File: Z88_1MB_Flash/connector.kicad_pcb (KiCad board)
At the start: 2 copper layers, 50.6 x 53.5 mm, 10 parts, among them J1 Conn_Z88, U1 AM29F080-120EC

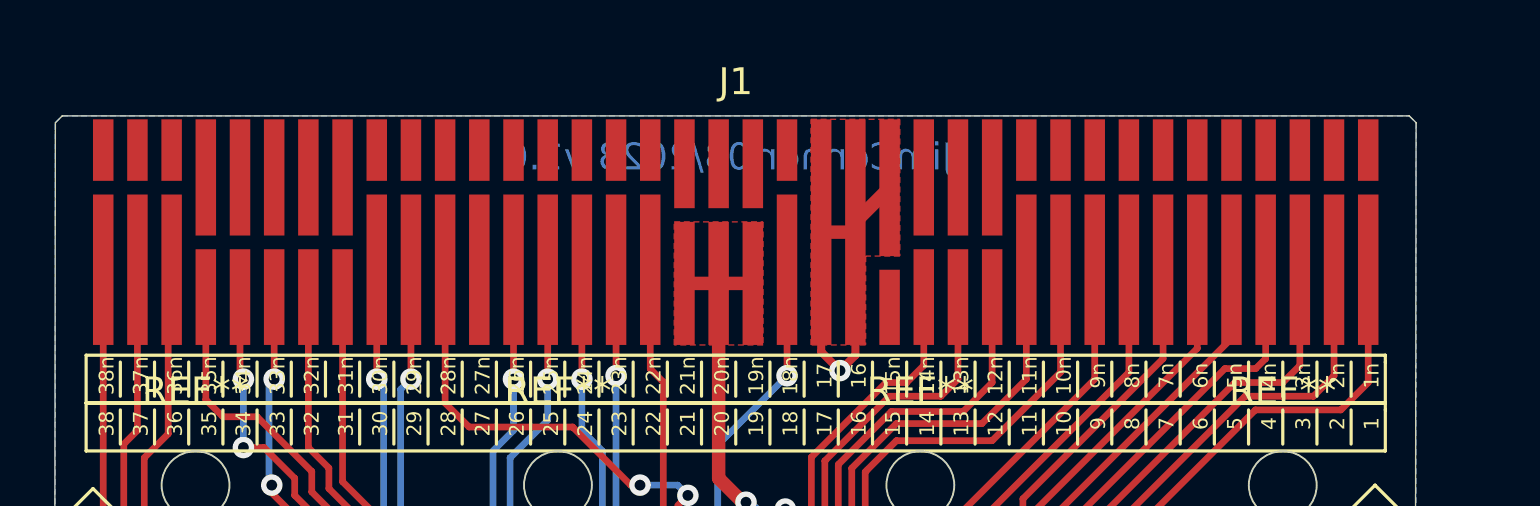
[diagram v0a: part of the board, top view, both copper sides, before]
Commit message: Correct pitch on Z88_connector.
Pads now spaced on 1.25mm instead of 1.27mm spacing.
Pad sizes changed to match the genuine Cambridge cartridge I have.
Sizes nicely in convienent 2m,3mm, 4mm sizing with 0.5mm gap.
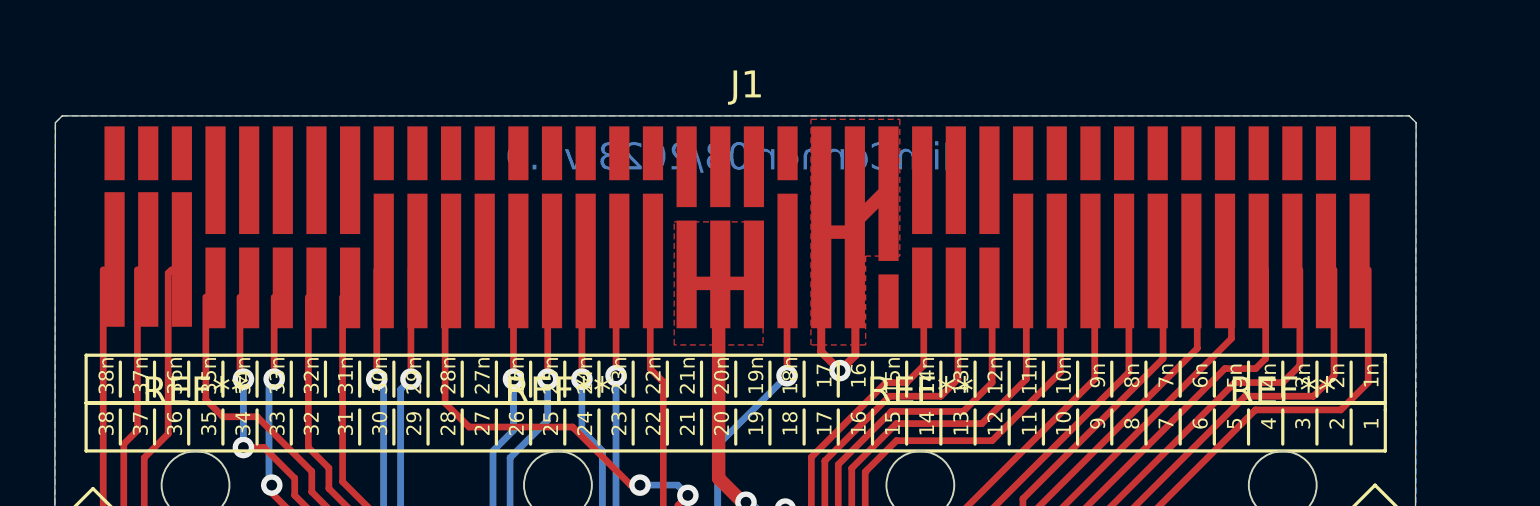
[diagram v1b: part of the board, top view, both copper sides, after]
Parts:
- moved J1 0.44 mm to (117.9, 64.4)

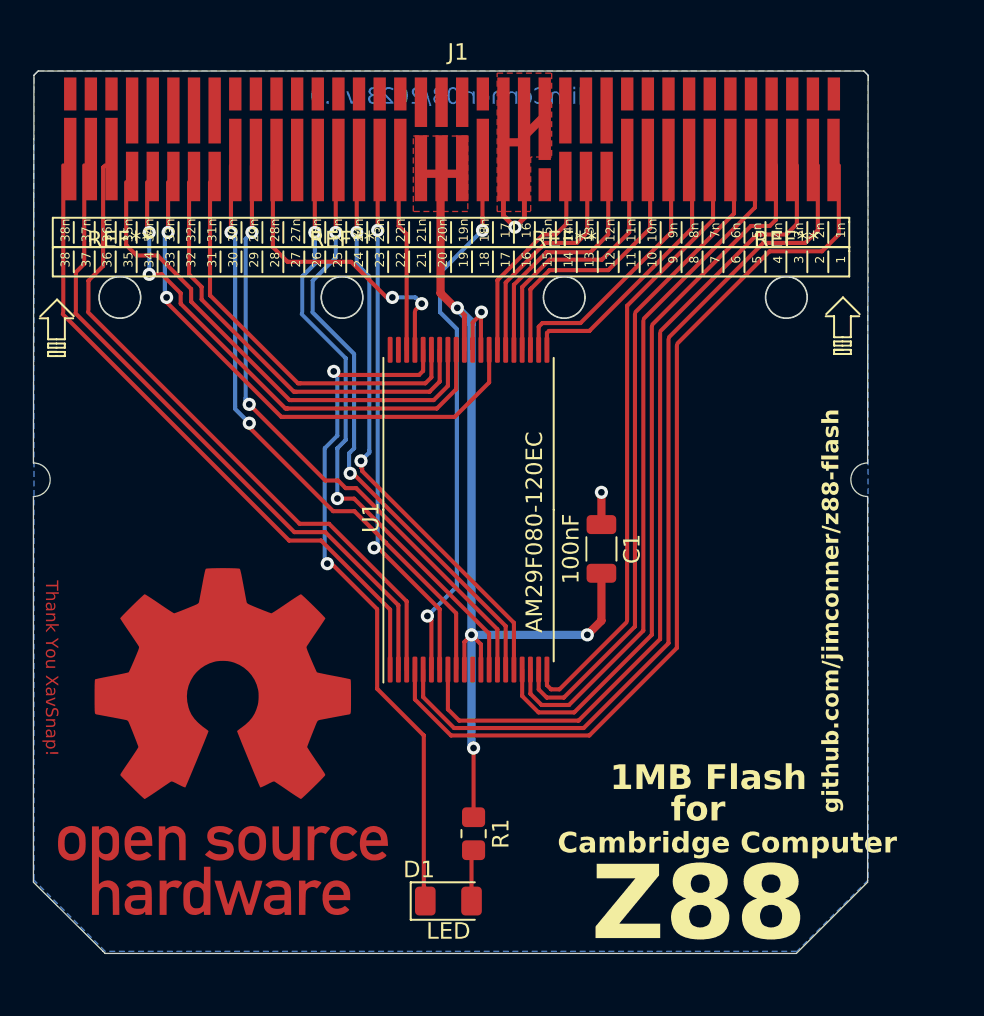
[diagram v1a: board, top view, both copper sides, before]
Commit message: Add support for using 2 x 512KB SRAM chips instead of 1MB Flash.
The board can now be used either as a 1MB Flash store, 512KB RAM or 1MB
RAM.
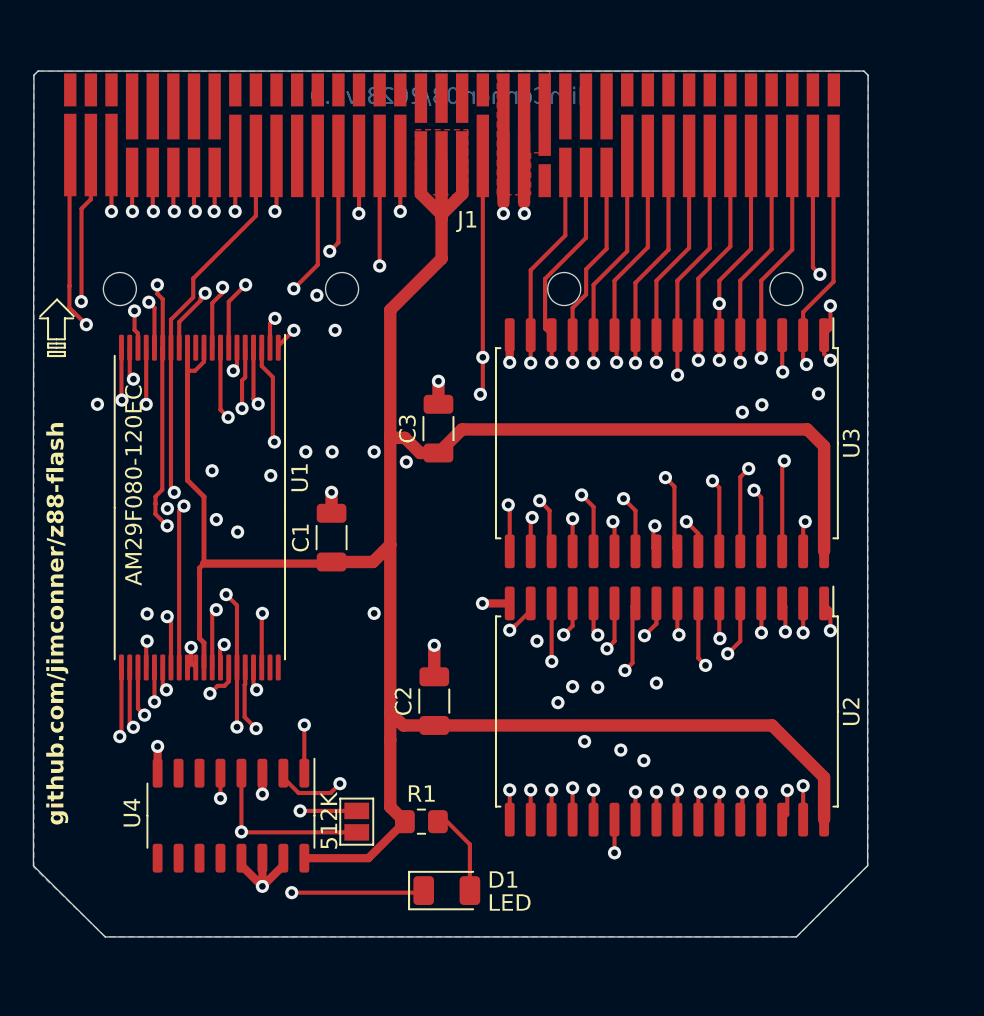
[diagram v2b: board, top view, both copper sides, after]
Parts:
- removed G***: LOGO, Z88_Connector:OSHW_Logo
- removed REF** (x4): MountingHole_2.5mm, MountingHole:MountingHole_2.5mm
- added 512K: 512KB RAM, Jumper:SolderJumper-2_P1.3mm_Open_Pad1.0x1.5mm, F.Cu at (135.3, 108.5)
- added C2: 100nF, Capacitor_SMD:C_1206_3216Metric, F.Cu at (140.0, 101.2)
- added C3: 100nF, Capacitor_SMD:C_1206_3216Metric, F.Cu at (140.2, 84.7)
- added U2: HY628400A LLG-70, Package_SO:SSOP-32_11.305x20.495mm_P1.27mm, F.Cu at (154.1, 101.8)
- added U3: HY628400A LLG-70, Package_SO:SSOP-32_11.305x20.495mm_P1.27mm, F.Cu at (154.1, 85.5)
- added U4: 74LS139, Package_SO:SO-16_3.9x9.9mm_P1.27mm, F.Cu at (127.6, 108.1)
- moved C1 16.4 mm to (133.7, 91.3), turned to 90 degrees
- moved U1 16.3 mm to (125.8, 89.4), turned to -90 degrees
- moved R1 3.24 mm to (139.2, 108.5), turned to 0 degrees
- moved D1 0.64 mm to (140.7, 112.6)
- moved J1 0.25 mm to (117.9, 64.1)
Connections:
- C1 pad 1: GND -> VCC
- C1 pad 2: VCC -> GND
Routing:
- net VCC: track 61.1 -> 154.9 mm, vias 4 -> 0
- net /WEL: track 11.4 -> 85.7 mm, vias 0 -> 6
- net /ROE: track 18.2 -> 79.7 mm, vias 2 -> 5
- net /A3: track 16.3 -> 77.2 mm, vias 0 -> 4
- net /A2: track 15.9 -> 75.8 mm, vias 0 -> 4
- net /D7: track 24.3 -> 81.1 mm, vias 0 -> 6
- net /A17: track 39.9 -> 93.3 mm, vias 0 -> 5
- net /A1: track 16.3 -> 69.2 mm, vias 0 -> 4
- net /D6: track 26.3 -> 77.9 mm, vias 0 -> 5
- net /A9: track 36.2 -> 86.1 mm, vias 2 -> 5
- net /A13: track 32.3 -> 81.6 mm, vias 2 -> 5
- net /D5: track 30.2 -> 79.2 mm, vias 0 -> 6
- net /D0: track 14.1 -> 63.0 mm, vias 0 -> 4
- net /A8: track 34.9 -> 82.9 mm, vias 2 -> 6
- net /A0: track 15.7 -> 62.6 mm, vias 0 -> 3
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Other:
- board size 50.6 x 53.5 mm -> 50.6 x 52.5 mm
- copper layers 2 -> 4
- board text added: "JimConner 03/2023 v2.0"
- board text removed: "1"
- board text removed: "10"
- board text removed: "10n"
- board text removed: "11"
- board text removed: "11n"
- board text removed: "12"
- board text removed: "12n"
- board text removed: "13"
- board text removed: "13n"
- board text removed: "14"
- board text removed: "14n"
- board text removed: "15"
- board text removed: "15n"
- board text removed: "16"
- board text removed: "17"
- board text removed: "18"
- board text removed: "18n"
- board text removed: "19"
- board text removed: "19n"
- board text removed: "1MB Flash"
- board text removed: "1n"
- board text removed: "2"
- board text removed: "20"
- board text removed: "20n"
- board text removed: "21"
- board text removed: "21n"
- board text removed: "22"
- board text removed: "22n"
- board text removed: "23"
- board text removed: "23n"
- board text removed: "24"
- board text removed: "24n"
- board text removed: "25"
- board text removed: "25n"
- board text removed: "26"
- board text removed: "26n"
- board text removed: "27"
- board text removed: "27n"
- board text removed: "28"
- board text removed: "28n"
- board text removed: "29"
- board text removed: "29n"
- board text removed: "2n"
- board text removed: "3"
- board text removed: "30"
- board text removed: "30n"
- board text removed: "31"
- board text removed: "31n"
- board text removed: "32"
- board text removed: "32n"
- board text removed: "33"
- board text removed: "33n"
- board text removed: "34"
- board text removed: "34n"
- board text removed: "35"
- board text removed: "35n"
- board text removed: "36"
- board text removed: "36n"
- board text removed: "37"
- board text removed: "37n"
- board text removed: "38"
- board text removed: "38n"
- board text removed: "3n"
- board text removed: "4"
- board text removed: "4n"
- board text removed: "5"
- board text removed: "5n"
- board text removed: "6"
- board text removed: "6n"
- board text removed: "7"
- board text removed: "7n"
- board text removed: "8"
- board text removed: "8n"
- board text removed: "9"
- board text removed: "9n"
- board text removed: "Cambridge Computer"
- board text removed: "JimConner 03/2023 v1.0"
- board text removed: "Thank You XavSnap!"
- board text removed: "Z88"
- board text removed: "for"
